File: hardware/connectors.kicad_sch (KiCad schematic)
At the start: 27 parts, among them J1 Kenwood-2.5, J10 UART, J11 Radio_Opt, J12 Speaker, J13 KH-RJ45-58-8P8C, J2 USB_C, J301 +12V, J301 OLED, J412 Hirose FH12-26S-0.5SH(55), J413 Molex 532610271, J5 Kenwood-3.5, J7 Radio, J9 STLink, U401 USBLC6-2SC6

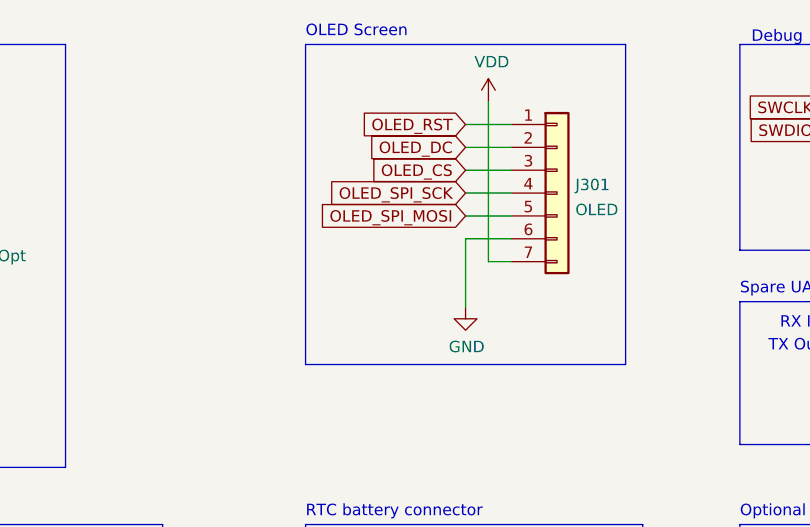
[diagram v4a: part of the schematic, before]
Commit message: Updated various symbols attributes
Updated various components (mostly LEDs and switches) to simplify the BOM and make it more easily readable.
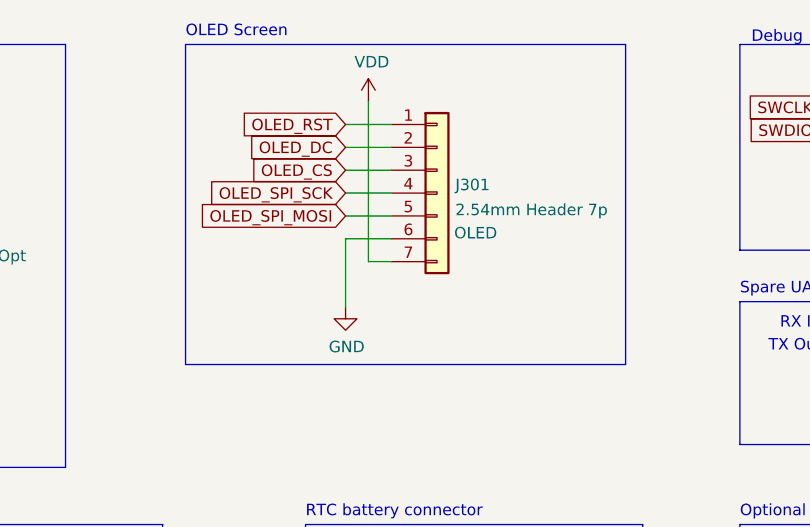
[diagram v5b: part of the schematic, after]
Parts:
- J301: value OLED -> 2.54mm Header 7p; Comment (none) -> OLED
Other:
- moved on the sheet: J301
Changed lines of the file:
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@@
     (stroke (width 0) (type default))
   )
-  (wire (pts (xy 153.67 42.545) (xy 151.13 42.545))
+  (wire (pts (xy 140.335 42.545) (xy 137.795 42.545))
     (stroke (width 0) (type solid))
   )
@@
     (stroke (width 0) (type default))
   )
-  (wire (pts (xy 151.13 42.545) (xy 151.13 24.765))
+  (wire (pts (xy 137.795 42.545) (xy 137.795 24.765))
     (stroke (width 0) (type solid))
   )
@@
     (stroke (width 0) (type default))
   )
-  (wire (pts (xy 148.59 29.845) (xy 153.67 29.845))
+  (wire (pts (xy 135.255 29.845) (xy 140.335 29.845))
     (stroke (width 0) (type solid))
   )
@@
     (stroke (width 0) (type default))
   )
-  (wire (pts (xy 148.59 34.925) (xy 153.67 34.925))
+  (wire (pts (xy 135.255 34.925) (xy 140.335 34.925))
     (stroke (width 0) (type solid))
   )
@@
     (stroke (width 0) (type solid))
   )
-  (wire (pts (xy 153.67 40.005) (xy 148.59 40.005))
+  (wire (pts (xy 140.335 40.005) (xy 135.255 40.005))
     (stroke (width 0) (type solid))
   )
@@
     (stroke (width 0) (type default))
   )
-  (wire (pts (xy 148.59 27.305) (xy 153.67 27.305))
+  (wire (pts (xy 135.255 27.305) (xy 140.335 27.305))
     (stroke (width 0) (type solid))
   )
@@
     (stroke (width 0) (type solid))
   )
-  (wire (pts (xy 148.59 40.005) (xy 148.59 47.625))
+  (wire (pts (xy 135.255 40.005) (xy 135.255 47.625))
     (stroke (width 0) (type solid))
   )
@@
     (stroke (width 0) (type default))
   )
-  (wire (pts (xy 148.59 37.465) (xy 153.67 37.465))
+  (wire (pts (xy 135.255 37.465) (xy 140.335 37.465))
     (stroke (width 0) (type solid))
   )
@@
     (stroke (width 0) (type default))
   )
-  (wire (pts (xy 148.59 32.385) (xy 153.67 32.385))
+  (wire (pts (xy 135.255 32.385) (xy 140.335 32.385))
     (stroke (width 0) (type solid))
   )
@@
     (fill (type none))
   )
-  (rectangle (start 130.81 18.415) (end 166.37 53.975)
+  (rectangle (start 117.475 18.415) (end 166.37 53.975)
     (stroke (width 0) (type default))
     (fill (type none))
@@
     (effects (font (size 1.27 1.27)) (justify left bottom))
   )
-  (text "OLED Screen" (at 130.81 17.78 0)
+  (text "OLED Screen" (at 117.475 17.78 0)
     (effects (font (size 1.27 1.27)) (justify left bottom))
   )
@@
     )
   )
-  (global_label "OLED_DC" (shape input) (at 148.59 29.845 180) (fields_autoplaced)
-    (effects (font (size 1.27 1.27)) (justify right))
-    (property "Intersheetrefs" "${INTERSHEET_REFS}" (at 138.0314 29.7656 0)
-      (effects (font (size 1.27 1.27)) (justify right) hide)
-    )
-  )
-  (global_label "OLED_SPI_MOSI" (shape input) (at 148.59 37.465 180) (fields_autoplaced)
-    (effects (font (size 1.27 1.27)) (justify right))
-    (property "Intersheetrefs" "${INTERSHEET_REFS}" (at 131.9233 37.3856 0)
-      (effects (font (size 1.27 1.27)) (justify right) hide)
-    )
-  )
-  (global_label "OLED_CS" (shape input) (at 148.59 32.385 180) (fields_autoplaced)
-    (effects (font (size 1.27 1.27)) (justify right))
-    (property "Intersheetrefs" "${INTERSHEET_REFS}" (at 138.0918 32.3056 0)
+  (global_label "OLED_DC" (shape input) (at 135.255 29.845 180) (fields_autoplaced)
+    (effects (font (size 1.27 1.27)) (justify right))
+    (property "Intersheetrefs" "${INTERSHEET_REFS}" (at 124.6964 29.7656 0)
+      (effects (font (size 1.27 1.27)) (justify right) hide)
+    )
+  )
+  (global_label "OLED_SPI_MOSI" (shape input) (at 135.255 37.465 180) (fields_autoplaced)
+    (effects (font (size 1.27 1.27)) (justify right))
+    (property "Intersheetrefs" "${INTERSHEET_REFS}" (at 118.5883 37.3856 0)
+      (effects (font (size 1.27 1.27)) (justify right) hide)
+    )
+  )
+  (global_label "OLED_CS" (shape input) (at 135.255 32.385 180) (fields_autoplaced)
+    (effects (font (size 1.27 1.27)) (justify right))
+    (property "Intersheetrefs" "${INTERSHEET_REFS}" (at 124.7568 32.3056 0)
       (effects (font (size 1.27 1.27)) (justify right) hide)
     )
@@
     )
   )
-  (global_label "OLED_SPI_SCK" (shape input) (at 148.59 34.925 180) (fields_autoplaced)
-    (effects (font (size 1.27 1.27)) (justify right))
-    (property "Intersheetrefs" "${INTERSHEET_REFS}" (at 132.7699 34.8456 0)
+  (global_label "OLED_SPI_SCK" (shape input) (at 135.255 34.925 180) (fields_autoplaced)
+    (effects (font (size 1.27 1.27)) (justify right))
+    (property "Intersheetrefs" "${INTERSHEET_REFS}" (at 119.4349 34.8456 0)
       (effects (font (size 1.27 1.27)) (justify right) hide)
     )
@@
     )
   )
-  (global_label "OLED_RST" (shape input) (at 148.59 27.305 180) (fields_autoplaced)
-    (effects (font (size 1.27 1.27)) (justify right))
-    (property "Intersheetrefs" "${INTERSHEET_REFS}" (at 137.1242 27.2256 0)
+  (global_label "OLED_RST" (shape input) (at 135.255 27.305 180) (fields_autoplaced)
+    (effects (font (size 1.27 1.27)) (justify right))
+    (property "Intersheetrefs" "${INTERSHEET_REFS}" (at 123.7892 27.2256 0)
       (effects (font (size 1.27 1.27)) (justify right) hide)
     )
@@
     )
   )
-  (symbol (lib_id "power:VDD") (at 151.13 24.765 0) (unit 1)
-    (in_bom yes) (on_board yes) (dnp no)
-    (property "Reference" "#PWR0312" (at 151.13 28.575 0)
-      (effects (font (size 1.27 1.27)) hide)
-    )
-    (property "Value" "VDD" (at 151.511 20.3708 0)
-      (effects (font (size 1.27 1.27)))
-    )
-    (property "Footprint" "" (at 151.13 24.765 0)
-      (effects (font (size 1.27 1.27)) hide)
-    )
-    (property "Datasheet" "" (at 151.13 24.765 0)
+  (symbol (lib_id "power:VDD") (at 137.795 24.765 0) (unit 1)
+    (in_bom yes) (on_board yes) (dnp no)
+    (property "Reference" "#PWR0312" (at 137.795 28.575 0)
+      (effects (font (size 1.27 1.27)) hide)
+    )
+    (property "Value" "VDD" (at 138.176 20.3708 0)
+      (effects (font (size 1.27 1.27)))
+    )
+    (property "Footprint" "" (at 137.795 24.765 0)
+      (effects (font (size 1.27 1.27)) hide)
+    )
+    (property "Datasheet" "" (at 137.795 24.765 0)
       (effects (font (size 1.27 1.27)) hide)
     )
@@
     )
   )
-  (symbol (lib_id "power:GND") (at 148.59 47.625 0) (unit 1)
-    (in_bom yes) (on_board yes) (dnp no)
-    (property "Reference" "#PWR0310" (at 148.59 53.975 0)
-      (effects (font (size 1.27 1.27)) hide)
-    )
-    (property "Value" "GND" (at 148.717 52.0192 0)
-      (effects (font (size 1.27 1.27)))
-    )
-    (property "Footprint" "" (at 148.59 47.625 0)
-      (effects (font (size 1.27 1.27)) hide)
-    )
-    (property "Datasheet" "" (at 148.59 47.625 0)
+  (symbol (lib_id "power:GND") (at 135.255 47.625 0) (unit 1)
+    (in_bom yes) (on_board yes) (dnp no)
+    (property "Reference" "#PWR0310" (at 135.255 53.975 0)
+      (effects (font (size 1.27 1.27)) hide)
+    )
+    (property "Value" "GND" (at 135.382 52.0192 0)
+      (effects (font (size 1.27 1.27)))
+    )
+    (property "Footprint" "" (at 135.255 47.625 0)
+      (effects (font (size 1.27 1.27)) hide)
+    )
+    (property "Datasheet" "" (at 135.255 47.625 0)
       (effects (font (size 1.27 1.27)) hide)
     )
@@
     )
   )
-  (symbol (lib_id "Connector_Generic:Conn_01x07") (at 158.75 34.925 0) (unit 1)
-    (in_bom yes) (on_board yes) (dnp no) (fields_autoplaced)
-    (property "Reference" "J301" (at 160.7821 34.0165 0)
+  (symbol (lib_id "Connector_Generic:Conn_01x07") (at 145.415 34.925 0) (unit 1)
+    (in_bom yes) (on_board yes) (dnp no)
+    (property "Reference" "J301" (at 147.4471 34.0165 0)
       (effects (font (size 1.27 1.27)) (justify left))
     )
-    (property "Value" "OLED" (at 160.7821 36.7916 0)
+    (property "Value" "2.54mm Header 7p" (at 147.4471 36.7916 0)
       (effects (font (size 1.27 1.27)) (justify left))
     )
-    (property "Footprint" "Connector_PinHeader_2.54mm:PinHeader_1x07_P2.54mm_Vertical" (at 158.75 34.925 0)
-      (effects (font (size 1.27 1.27)) hide)
-    )
-    (property "Datasheet" "~" (at 158.75 34.925 0)
-      (effects (font (size 1.27 1.27)) hide)
-    )
-    (property "MPN" "PZ254V-11-07P" (at 158.75 34.925 0)
-      (effects (font (size 1.27 1.27)) hide)
-    )
-    (property "LCSC Part #" "C492406" (at 158.75 34.925 0)
-      (effects (font (size 1.27 1.27)) hide)
-    )
-    (pin "1")
+    (property "Footprint" "Connector_PinHeader_2.54mm:PinHeader_1x07_P2.54mm_Vertical" (at 145.415 34.925 0)
+      (effects (font (size 1.27 1.27)) hide)
+    )
+    (property "Datasheet" "~" (at 145.415 34.925 0)
+      (effects (font (size 1.27 1.27)) hide)
+    )
+    (property "MPN" "PZ254V-11-07P" (at 145.415 34.925 0)
+      (effects (font (size 1.27 1.27)) hide)
+    )
+    (property "LCSC Part #" "C492406" (at 145.415 34.925 0)
+      (effects (font (size 1.27 1.27)) hide)
+    )
+    (property "Comment" "OLED" (at 147.32 39.37 0)
+      (effects (font (size 1.27 1.27)) (justify left))
+    )
+    (pin "1")

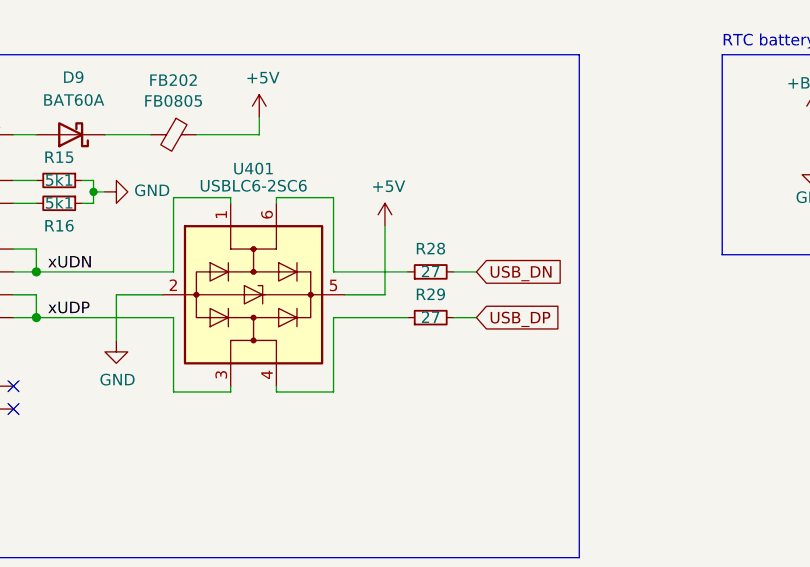
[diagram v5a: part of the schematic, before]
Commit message: Removed USB serial resistors
Those are not needed on STM32F405 series line
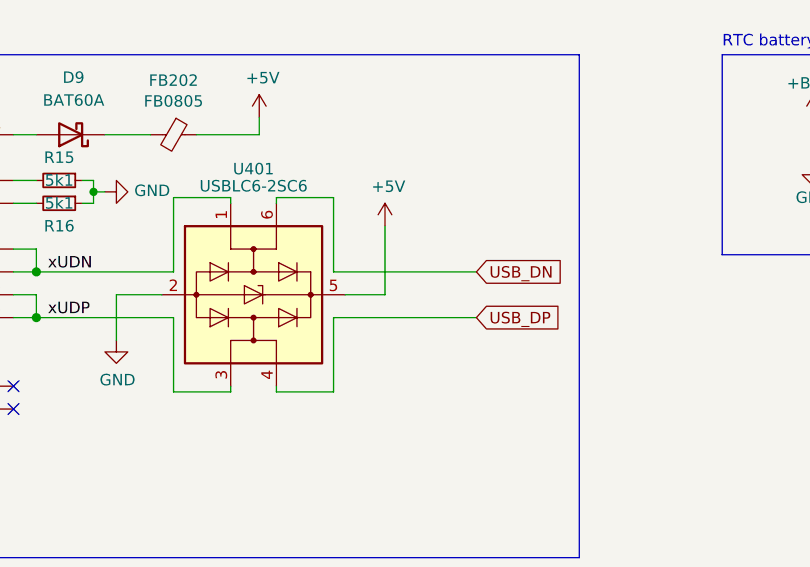
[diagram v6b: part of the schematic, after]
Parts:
- removed R28, R29: 27, Resistor_SMD:R_0603_1608Metric, symbol Device:R_Small
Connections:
- net USB_DN: now also U401.6 (I/O1)
- net USB_DP: now also U401.4 (I/O2)
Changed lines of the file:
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@@
     (stroke (width 0) (type default))
-  )
-  (wire (pts (xy 87.63 100.965) (xy 95.885 100.965))
-    (stroke (width 0) (type solid))
   )
   (wire (pts (xy 182.88 97.155) (xy 182.88 97.79))
@@
     (stroke (width 0) (type solid))
   )
-  (wire (pts (xy 100.965 95.885) (xy 103.505 95.885))
-    (stroke (width 0) (type solid))
-  )
   (wire (pts (xy 40.64 46.99) (xy 60.96 46.99))
     (stroke (width 0) (type default))
@@
     (stroke (width 0) (type default))
   )
-  (wire (pts (xy 87.63 95.885) (xy 95.885 95.885))
+  (wire (pts (xy 87.63 95.885) (xy 103.505 95.885))
     (stroke (width 0) (type solid))
   )
@@
     (stroke (width 0) (type default))
   )
-  (wire (pts (xy 100.965 100.965) (xy 103.505 100.965))
+  (wire (pts (xy 87.63 100.965) (xy 103.505 100.965))
     (stroke (width 0) (type solid))
   )
@@
     )
   )
-  (symbol (lib_id "Device:R_Small") (at 98.425 95.885 90) (unit 1)
-    (in_bom yes) (on_board yes) (dnp no)
-    (property "Reference" "R28" (at 98.425 93.345 90)
-      (effects (font (size 1.27 1.27)))
-    )
-    (property "Value" "27" (at 98.425 95.885 90)
-      (effects (font (size 1.27 1.27)))
-    )
-    (property "Footprint" "Resistor_SMD:R_0603_1608Metric" (at 98.425 95.885 0)
-      (effects (font (size 1.524 1.524)) hide)
-    )
-    (property "Datasheet" "" (at 98.425 95.885 0)
-      (effects (font (size 1.524 1.524)))
-    )
-    (property "MPN" "Generic R/27R/0603" (at 98.425 95.885 0)
-      (effects (font (size 1.27 1.27)) hide)
-    )
-    (pin "1")
-    (pin "2")
-    (instances
-      (project "M17-SmartMic"
-        (path "/59592280-3207-432b-a891-cd517ec5cf12/00000000-0000-0000-0000-0000612c95ef"
-          (reference "R28") (unit 1)
-        )
-        (path "/59592280-3207-432b-a891-cd517ec5cf12/7f9420e4-5dd1-4e05-8205-18dae2029540"
-          (reference "R403") (unit 1)
-        )
-      )
-    )
-  )
   (symbol (lib_name "GND_2") (lib_id "power:GND") (at 140.97 83.82 0) (unit 1)
     (in_bom yes) (on_board yes) (dnp no)
@@
         )
       )
-    )
-  )
-  (symbol (lib_id "Device:R_Small") (at 98.425 100.965 90) (unit 1)
-    (in_bom yes) (on_board yes) (dnp no)
-    (property "Reference" "R29" (at 98.425 98.425 90)
-      (effects (font (size 1.27 1.27)))
-    )
-    (property "Value" "27" (at 98.425 100.965 90)
-      (effects (font (size 1.27 1.27)))
-    )
-    (property "Footprint" "Resistor_SMD:R_0603_1608Metric" (at 98.425 100.965 0)
-      (effects (font (size 1.524 1.524)) hide)
-    )
-    (property "Datasheet" "" (at 98.425 100.965 0)
-      (effects (font (size 1.524 1.524)))
-    )
-    (property "MPN" "Generic R/27R/0603" (at 98.425 100.965 0)
-      (effects (font (size 1.27 1.27)) hide)
-    )
-    (pin "1")
-    (pin "2")
-    (instances
-      (project "M17-SmartMic"
-        (path "/59592280-3207-432b-a891-cd517ec5cf12/00000000-0000-0000-0000-0000612c95ef"
-          (reference "R29") (unit 1)
-        )
-        (path "/59592280-3207-432b-a891-cd517ec5cf12/7f9420e4-5dd1-4e05-8205-18dae2029540"
-          (reference "R404") (unit 1)
-        )
-      )
